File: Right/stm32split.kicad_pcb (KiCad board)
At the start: 2 copper layers, 152.4 x 110.7 mm, 93 parts, among them J1 Conn_01x04, SW1 SW_Push, SW10 SW_Push, SW11 SW_Push, SW12 SW_Push, SW13 SW_Push, SW14 SW_Push, SW15 SW_Push, SW16 SW_Push, SW17 SW_Push, SW18 SW_Push, SW19 SW_Push, SW2 SW_Push, SW20 SW_Push, SW21 SW_Push, SW22 SW_Push, SW23 SW_Push, SW24 SW_Push, SW25 SW_Push, SW26 SW_Push, SW27 SW_Push, SW28 SW_Push, SW29 SW_Push, SW3 SW_Push, SW30 SW_Push, SW31 SW_Push, SW4 SW_Push, SW5 SW_Push, SW6 SW_Push, SW7 SW_Push, SW8 SW_Push, SW9 SW_Push, U1 SRV05-4, U2 STM32F103CBTx, U3 XC6206PxxxMR, Y1 8MHz

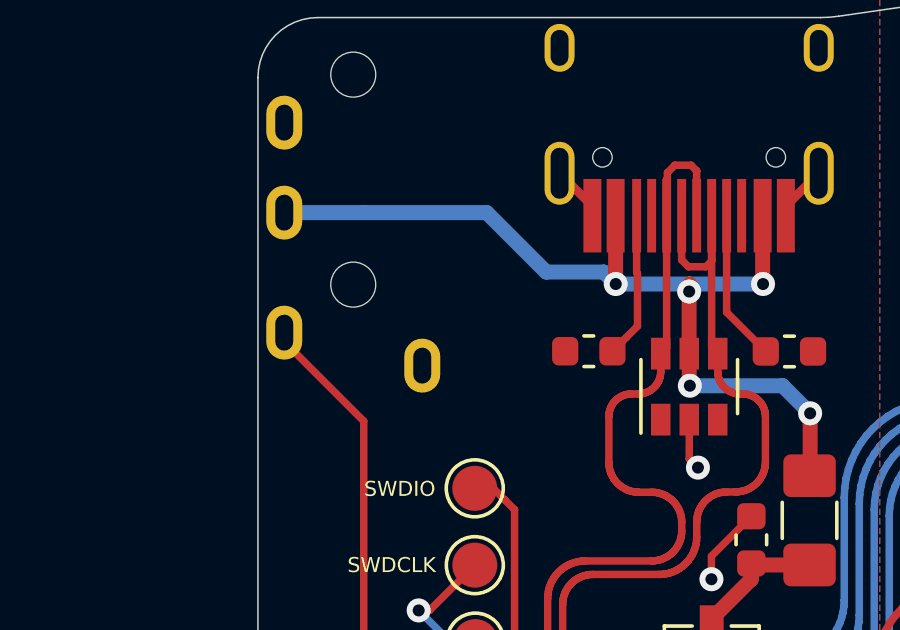
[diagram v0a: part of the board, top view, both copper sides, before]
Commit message: changed vbus pin
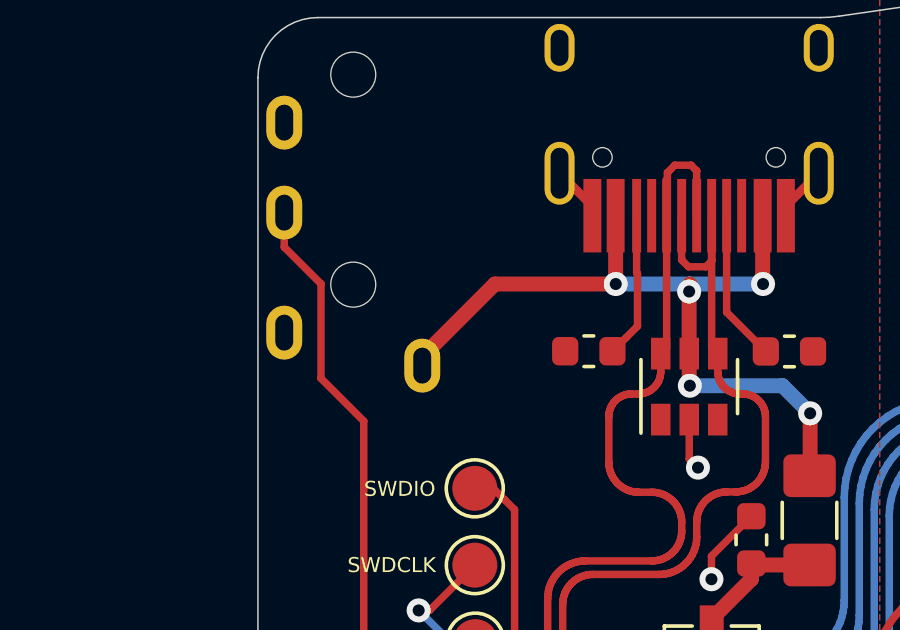
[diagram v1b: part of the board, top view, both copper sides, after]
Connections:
- J1 pad 1: Net-(J1-Pad1) -> GND
- J1 pad 2: VBUS -> SPLITHANDPIN
- J1 pad 3: SPLITHANDPIN -> (no net)
- J1 pad 4: GND -> VBUS
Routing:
- net VBUS: track 31.4 -> 27.1 mm
- net SPLITHANDPIN: track 24.8 -> 28.8 mm
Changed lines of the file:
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@@
     (thickness 1.6)
     (drawings 245)
-    (tracks 3824)
+    (tracks 3825)
     (zones 0)
     (modules 93)
-    (nets 82)
+    (nets 81)
   )
   (page A4)
@@
     (mod_text_size 1 1)
     (mod_text_width 0.15)
-    (pad_size 2 2)
-    (pad_drill 1)
+    (pad_size 1.8 1.2)
+    (pad_drill 1.2)
     (pad_to_mask_clearance 0.051)
     (solder_mask_min_width 0.25)
@@
   (net 79 SOFTSERIALPIN)
   (net 80 SPLITHANDPIN)
-  (net 81 "Net-(J1-Pad1)")
   (net_class Default "This is the default net class."
     (clearance 0.2)
@@
     (add_net "Net-(D8-Pad2)")
     (add_net "Net-(D9-Pad2)")
-    (add_net "Net-(J1-Pad1)")
     (add_net "Net-(R1-Pad2)")
     (add_net "Net-(R2-Pad2)")
@@
     (pad "" np_thru_hole circle (at 1.6 0 270) (size 1.5 1.5) (drill 1.5) (layers *.Cu *.Mask))
     (pad 4 thru_hole oval (at 11.3 -2.3 270) (size 1.8 1.2) (drill oval 1.2 0.6) (layers *.Cu *.Mask)
-      (net 66 GND))
-    (pad 3 thru_hole oval (at 10.2 2.3 270) (size 1.8 1.2) (drill oval 1.2 0.6) (layers *.Cu *.Mask)
-      (net 80 SPLITHANDPIN))
-    (pad 2 thru_hole oval (at 6.2 2.3 270) (size 1.8 1.2) (drill oval 1.2 0.6) (layers *.Cu *.Mask)
       (net 65 VBUS))
+    (pad 3 thru_hole oval (at 10.2 2.3 270) (size 1.8 1.2) (drill oval 1.2 0.6) (layers *.Cu *.Mask))
+    (pad 2 thru_hole oval (at 6.2 2.3 270) (size 1.8 1.2) (drill oval 1.2 0.6) (layers *.Cu *.Mask)
+      (net 80 SPLITHANDPIN))
     (pad 1 thru_hole oval (at 3.2 2.3 270) (size 1.8 1.2) (drill oval 1.2 0.6) (layers *.Cu *.Mask)
-      (net 81 "Net-(J1-Pad1)"))
+      (net 66 GND))
   )
   (module Crystal:Crystal_SMD_5032-2Pin_5.0x3.2mm (layer F.Cu)
@@
   (segment (start 103.99625 60.30625) (end 104 60.31) (width 0.5) (layer B.Cu) (net 65))
   (via (at 104 60.31) (size 0.8) (drill 0.4) (layers F.Cu B.Cu) (net 65))
-  (segment (start 104 60.31) (end 103.600001 59.910001) (width 0.5) (layer B.Cu) (net 65))
-  (segment (start 103.600001 59.910001) (end 101.680001 59.910001) (width 0.5) (layer B.Cu) (net 65))
   (via (at 106.47 63.699998) (size 0.8) (drill 0.4) (layers F.Cu B.Cu) (net 65))
   (segment (start 106.45 63.679998) (end 106.47 63.699998) (width 0.5) (layer F.Cu) (net 65))
   (segment (start 106.45 62.63) (end 106.45 63.679998) (width 0.5) (layer F.Cu) (net 65))
   (segment (start 106.47 63.699998) (end 108.039998 63.699998) (width 0.5) (layer B.Cu) (net 65))
-  (segment (start 99.7 57.93) (end 95.6 57.93) (width 0.5) (layer B.Cu) (net 65))
-  (segment (start 101.680001 59.910001) (end 99.7 57.93) (width 0.5) (layer B.Cu) (net 65))
-  (segment (start 95.6 57.93) (end 92.95 57.93) (width 0.5) (layer B.Cu) (net 65))
   (via (at 110.48 64.62) (size 0.8) (drill 0.4) (layers F.Cu B.Cu) (net 65))
   (segment (start 109.559998 63.699998) (end 110.48 64.62) (width 0.5) (layer B.Cu) (net 65))
@@
   (segment (start 110.48 66.68) (end 110.46 66.7) (width 0.5) (layer F.Cu) (net 65))
   (segment (start 110.48 64.62) (end 110.48 66.68) (width 0.5) (layer F.Cu) (net 65))
+  (segment (start 97.55 62.73) (end 97.55 63.03) (width 0.5) (layer F.Cu) (net 65))
+  (segment (start 99.97 60.31) (end 97.55 62.73) (width 0.5) (layer F.Cu) (net 65))
+  (segment (start 104 60.31) (end 99.97 60.31) (width 0.5) (layer F.Cu) (net 65))
   (segment (start 109.67125 58.0325) (end 109.67125 57.7125) (width 0.3) (layer F.Cu) (net 66))
   (segment (start 109.67125 57.7125) (end 110.76625 56.6175) (width 0.3) (layer F.Cu) (net 66))
@@
   (segment (start 98.81875 83.80625) (end 97.98125 83.80625) (width 0.25) (layer F.Cu) (net 80))
   (segment (start 95.6 64.88) (end 95.6 81.425) (width 0.25) (layer F.Cu) (net 80))
-  (segment (start 92.95 62.23) (end 95.6 64.88) (width 0.25) (layer F.Cu) (net 80))
-  (segment (start 92.95 61.93) (end 92.95 62.23) (width 0.25) (layer F.Cu) (net 80))
+  (segment (start 92.95 61.93) (end 92.95 62.23) (width 0.25) (layer F.Cu) (net 0))
+  (segment (start 94.174999 60.304999) (end 92.95 59.08) (width 0.25) (layer F.Cu) (net 80))
+  (segment (start 92.95 59.08) (end 92.95 57.93) (width 0.25) (layer F.Cu) (net 80))
+  (segment (start 94.174999 63.454999) (end 94.174999 60.304999) (width 0.25) (layer F.Cu) (net 80))
+  (segment (start 95.6 64.88) (end 94.174999 63.454999) (width 0.25) (layer F.Cu) (net 80))
   (zone (net 66) (net_name GND) (layer B.Cu) (hatch edge 0.508)
     (connect_pads (clearance 0.508))
